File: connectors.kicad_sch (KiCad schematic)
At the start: 42 parts, among them J1 Molex_Nano-Fit_1x2_SMD_105430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, J2 Conn_FAKRA_59S2AQ-40MT5-Z_1, J3 Conn_FAKRA_59S2AQ-40MT5-Z_1, J4 Conn_FAKRA_59S2AQ-40MT5-Z_1, J5 Conn_FAKRA_59S2AQ-40MT5-Z_1, J6 Conn_FFC_WE_68715014522, U1 SN74LV1T125DBVR, U2 SN74LV1T125DBVR, U8 SN74LV1T125DBVR, U9 SN74LV1T125DBVR

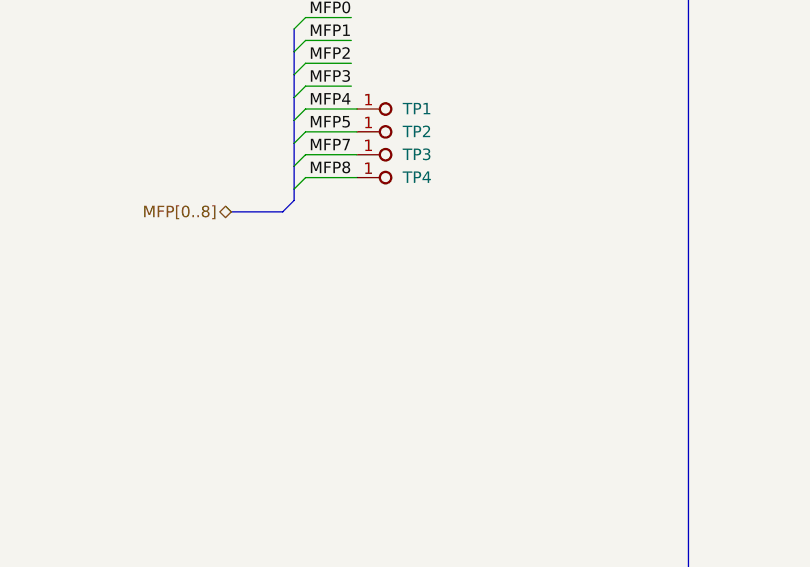
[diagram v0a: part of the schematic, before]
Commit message: Connectors: add GND testpoint
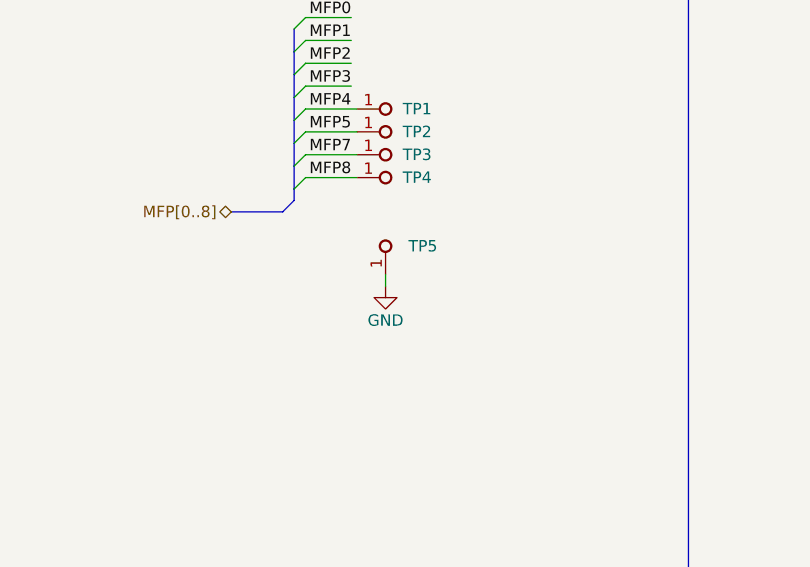
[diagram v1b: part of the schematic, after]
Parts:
- added TP5: TP_0.75mm_SMD, antmicro-footprints:TP_SMD_0.75mm, symbol antmicroTestPoints:TP_0.75mm_SMD
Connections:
- net GND: now also TP5.1
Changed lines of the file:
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@@
+    (stroke (width 0) (type default) (color 0 0 0 0))
+  )
+  (wire (pts (xy 56.515 215.9) (xy 56.515 217.17))
     (stroke (width 0) (type default) (color 0 0 0 0))
   )
@@
     )
     (property "License" "Apache-2.0" (id 5) (at 182.88 125.73 0)
+      (effects (font (size 1.27 1.27) (thickness 0.15)) (justify left bottom) hide)
+    )
+    (pin "1")
+  )
+  (symbol (lib_id "antmicropower:GND") (at 56.515 217.17 0) (unit 1)
+    (in_bom yes) (on_board yes)
+    (property "Reference" "#PWR0109" (id 0) (at 65.405 219.71 0)
+      (effects (font (size 1.27 1.27) (thickness 0.15)) (justify left bottom) hide)
+    )
+    (property "Value" "GND" (id 1) (at 56.515 220.98 0)
+      (effects (font (size 1.27 1.27) (thickness 0.15)))
+    )
+    (property "Footprint" "" (id 2) (at 65.405 224.79 0)
+      (effects (font (size 1.27 1.27) (thickness 0.15)) (justify left bottom) hide)
+    )
+    (property "Datasheet" "" (id 3) (at 65.405 229.87 0)
+      (effects (font (size 1.27 1.27) (thickness 0.15)) (justify left bottom) hide)
+    )
+    (property "Author" "Antmicro" (id 4) (at 65.405 224.79 0)
+      (effects (font (size 1.27 1.27) (thickness 0.15)) (justify left bottom) hide)
+    )
+    (property "License" "Apache-2.0" (id 5) (at 65.405 227.33 0)
       (effects (font (size 1.27 1.27) (thickness 0.15)) (justify left bottom) hide)
     )
@@
     (pin "2")
   )
+  (symbol (lib_id "antmicroTestPoints:TP_0.75mm_SMD") (at 56.515 215.9 90) (unit 1)
+    (in_bom yes) (on_board yes) (fields_autoplaced)
+    (property "Reference" "TP5" (id 0) (at 59.055 212.7249 90)
+      (effects (font (size 1.27 1.27) (thickness 0.15)) (justify right))
+    )
+    (property "Value" "TP_0.75mm_SMD" (id 1) (at 60.325 205.105 0)
+      (effects (font (size 1.27 1.27) (thickness 0.15)) (justify left bottom) hide)
+    )
+    (property "Footprint" "antmicro-footprints:TP_SMD_0.75mm" (id 2) (at 62.865 205.105 0)
+      (effects (font (size 1.27 1.27) (thickness 0.15)) (justify left bottom) hide)
+    )
+    (property "Datasheet" "" (id 3) (at 69.215 198.12 0)
+      (effects (font (size 1.27 1.27) (thickness 0.15)) (justify left bottom) hide)
+    )
+    (property "MPN" "" (id 4) (at 67.945 205.105 0)
+      (effects (font (size 1.27 1.27) (thickness 0.15)) (justify left bottom) hide)
+    )
+    (property "Manufacturer" "" (id 5) (at 62.865 205.105 0)
+      (effects (font (size 1.27 1.27) (thickness 0.15)) (justify left bottom) hide)
+    )
+    (property "Author" "Antmicro" (id 6) (at 65.405 205.105 0)
+      (effects (font (size 1.27 1.27) (thickness 0.15)) (justify left bottom) hide)
+    )
+    (property "License" "Apache-2.0" (id 7) (at 67.945 205.105 0)
+      (effects (font (size 1.27 1.27) (thickness 0.15)) (justify left bottom) hide)
+    )
+    (pin "1")
+  )
   (symbol (lib_id "antmicroFuses:F_3A_1206") (at 69.215 68.58 0) (unit 1)

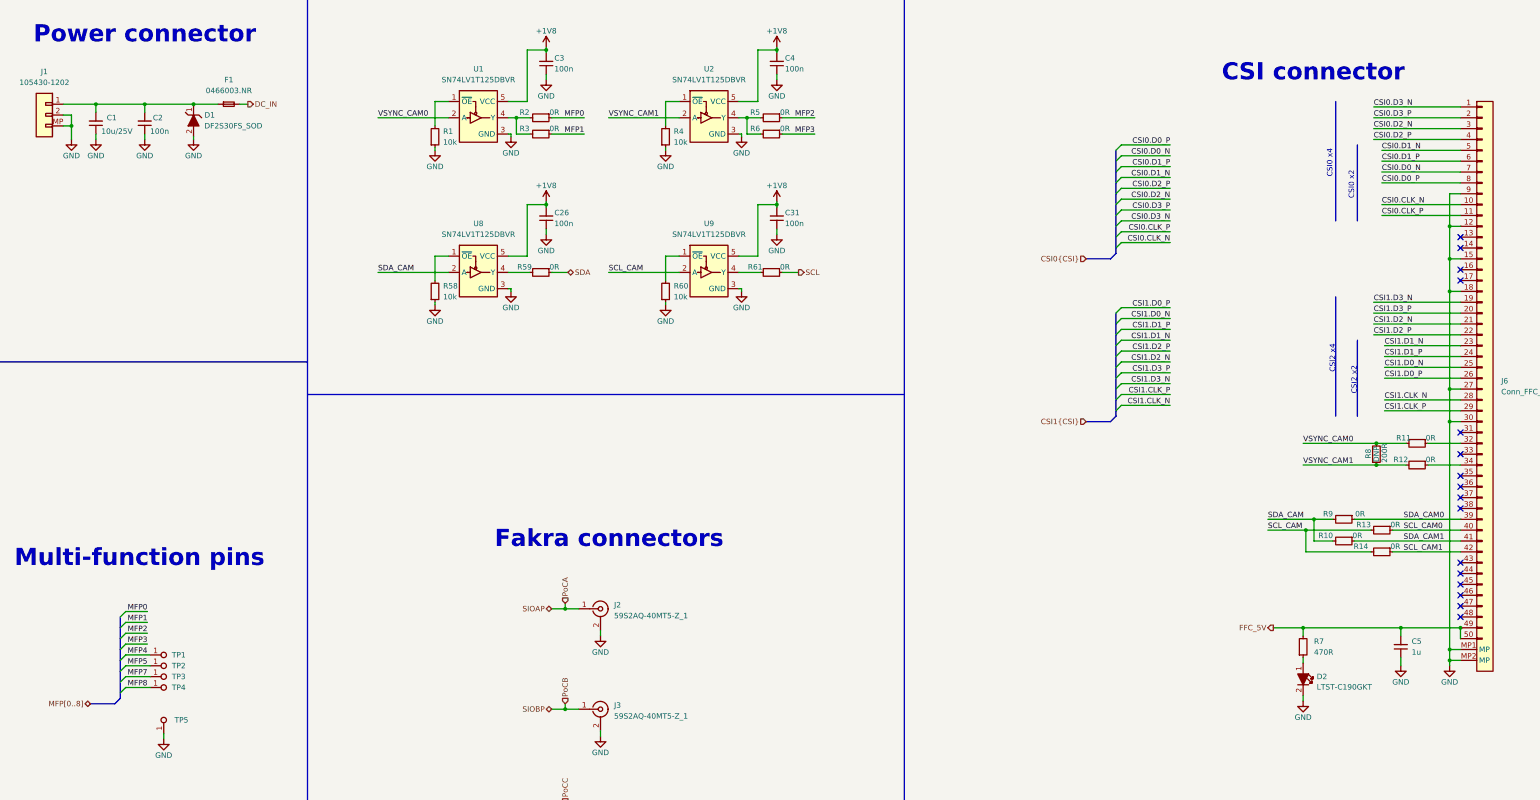
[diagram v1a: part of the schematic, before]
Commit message: Connectors: replace i2c buffer gate with proper level shifter, Power: add test points
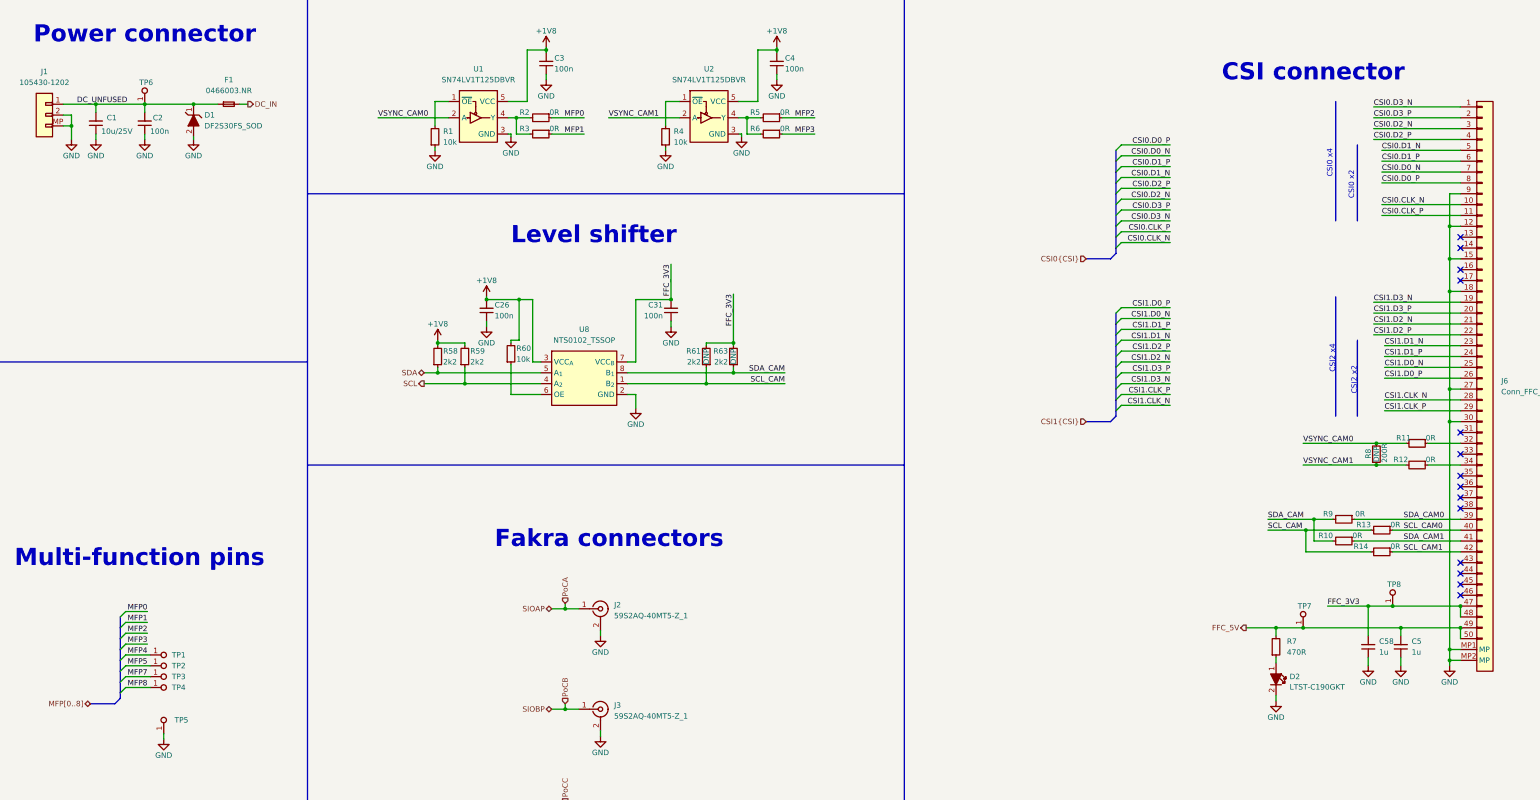
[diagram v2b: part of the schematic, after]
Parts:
- removed R58: R_10k_0402, antmicro-footprints:R_0402_1005Metric, symbol antmicroResistors0402:R_10k_0402
- removed R59, R61: R_0R_0402, antmicro-footprints:R_0402_1005Metric, symbol antmicroResistors0402:R_0R_0402
- removed U8, U9: SN74LV1T125DBVR, antmicro-footprints:SOT-23-5, symbol antmicroLogicBuffersDriversReceiversTransceivers:SN74LV1T125DBVR
- added C58: C_1u_0402, antmicro-footprints:C_0402_1005Metric, symbol antmicroCapacitors0402:C_1u_0402
- added R58, R59, R61, R63: R_2k2_0402, antmicro-footprints:R_0402_1005Metric, symbol antmicroResistors0402:R_2k2_0402
- added TP6, TP7, TP8: TP_0.75mm_SMD, antmicro-footprints:TP_SMD_0.75mm, symbol antmicroTestPoints:TP_0.75mm_SMD
- added U8: NTS0102_TSSOP, antmicro-footprints:TSSOP-8_3x3mm_P0.65mm, symbol antmicroLogicTranslatorsLevelShifters:NTS0102_TSSOP
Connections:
- net +1V8: now also R60.2, R58.2, R59.2, U8.3 (VCC_{A}); no longer C31.2
- net FFC_5V: now also TP7.1
- net GND: now also C58.1, U8.2 (GND); no longer R60.1
- net SCL: now also R59.1, U8.4 (A_{2})
- net SCL_CAM: now also R61.1, U8.1 (B_{2})
- net SDA: now also R58.1, U8.5 (A_{1})
- net SDA_CAM: now also R63.1, U8.8 (B_{1})
- net DC_UNFUSED: now reaches C1.2, C2.2, D1.1, F1.1, J1.1
- net DC_UNFUSED: now also TP6.1
- net FFC_3V3: now reaches J6.47
- net FFC_3V3: now also C31.2, J6.48, C58.2, R61.2, R63.2, TP8.1, U8.7 (VCC_{B})
- new net: R60.1, U8.6 (OE)
- no-connect marks 16 -> 14
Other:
- note added: "Level shifter"
- moved on the sheet: D2, R7

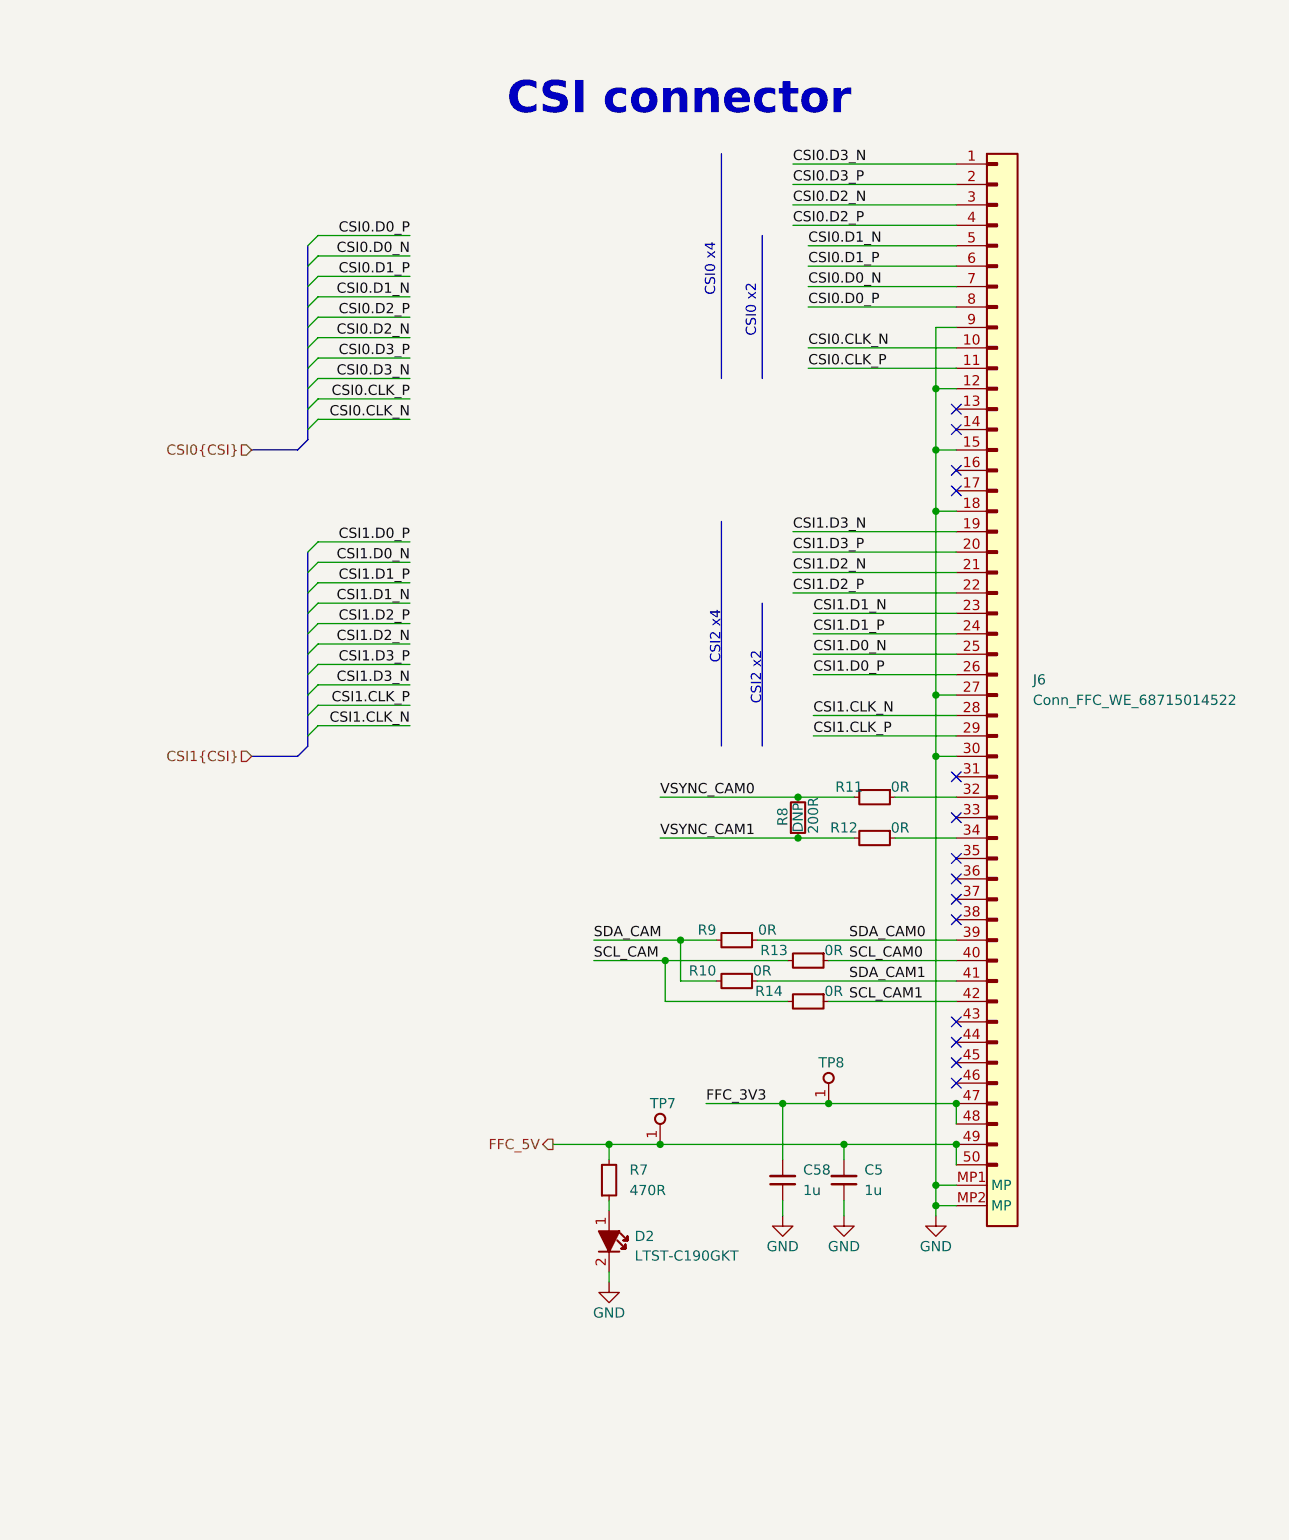
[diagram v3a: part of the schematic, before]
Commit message: Connectors: add TVS diodes to VSYNC, I2C and FFC power
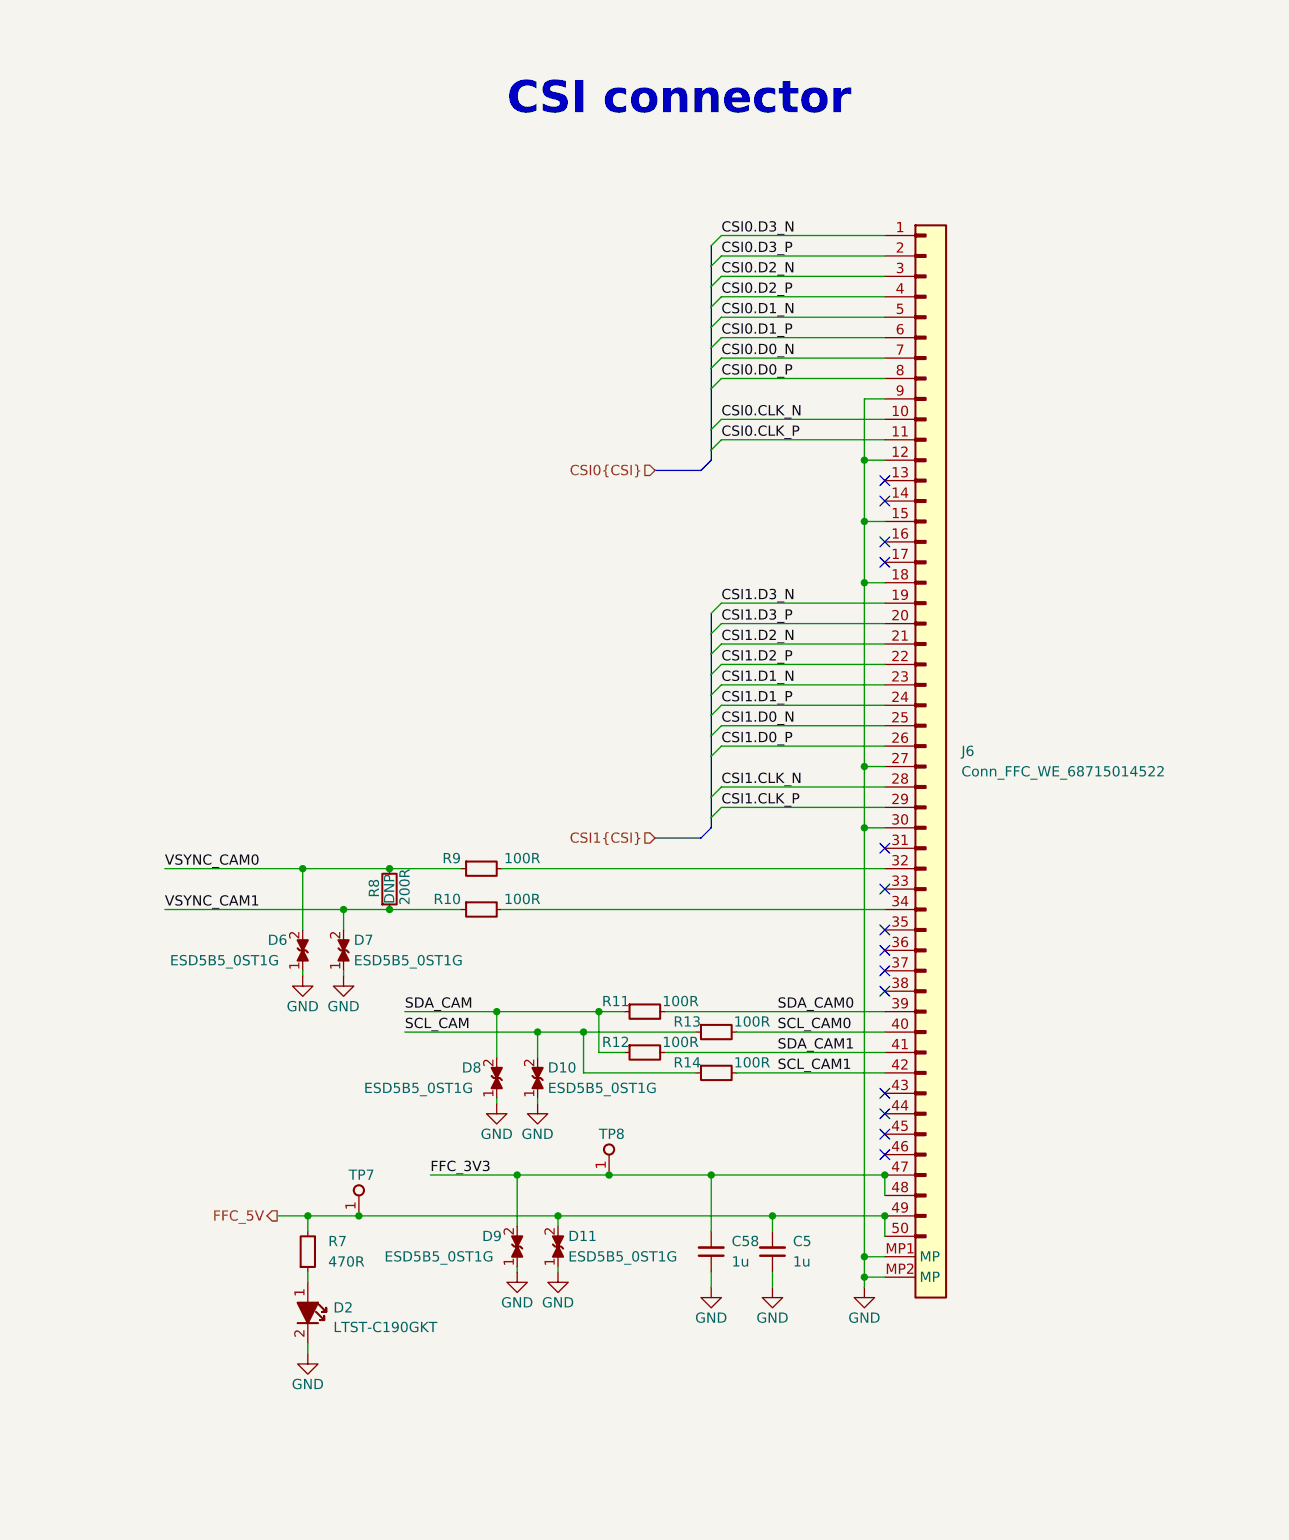
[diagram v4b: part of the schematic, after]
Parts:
- removed R10, R11, R12, R13, R14, R9: R_0R_0402, antmicro-footprints:R_0402_1005Metric, symbol antmicroResistors0402:R_0R_0402
- added D10, D11, D6, D7, D8, D9: ESD5B5_0ST1G, antmicro-footprints:SOD-523_NP, symbol antmicroTVSDiodes:ESD5B5_0ST1G
- added R10, R11, R12, R13, R14, R9: R_100R_0402, antmicro-footprints:R_0402_1005Metric, symbol antmicroResistors0402:R_100R_0402
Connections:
- net FFC_3V3: now also D9.2
- net FFC_5V: now also D11.2
- net GND: now also D10.1, D11.1, D6.1, D7.1, D8.1, D9.1
- net SCL_CAM: now also D10.2, R13.1, R14.1
- net SCL_CAM0: now also R13.2
- net SCL_CAM1: now also R14.2
- net SDA_CAM: now also D8.2, R11.1, R12.1
- net SDA_CAM0: now also R11.2
- net SDA_CAM1: now also R12.2
- net VSYNC_CAM0: now also D6.2, R9.1
- net VSYNC_CAM1: now also D7.2, R10.1
- net at J6.32: now also R9.2
- net at J6.34: now also R10.2
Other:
- note removed: "CSI0 x2"
- note removed: "CSI0 x4"
- note removed: "CSI2 x2"
- note removed: "CSI2 x4"
- moved on the sheet: C5, C58, D2, J6, R7, R8, TP7, TP8
